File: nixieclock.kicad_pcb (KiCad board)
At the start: 2 copper layers, 146.5 x 85 mm, 56 parts, among them Q1 MMBTA42, Q2 FDS2672CT, Q3 SS8050, U1 UCC3803, U2 K155NA1, U3 PicoW, U4 K155NA1, U5 K155NA1, U6 K155NA1, U7 K155NA1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

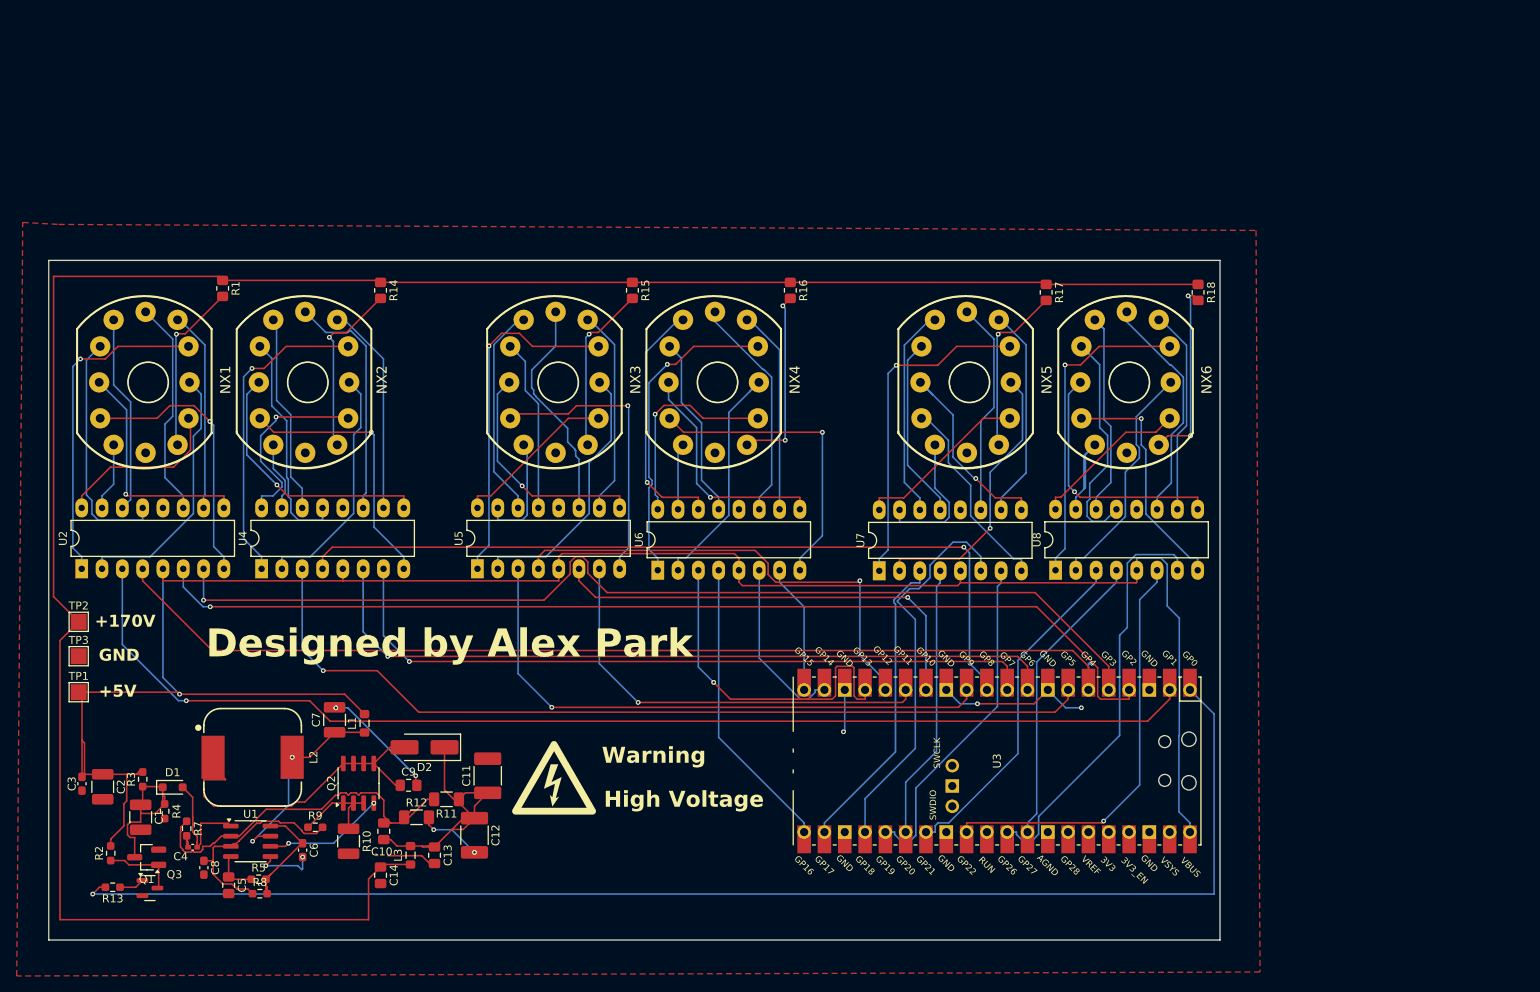
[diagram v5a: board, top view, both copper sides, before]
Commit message: updates to silk screen
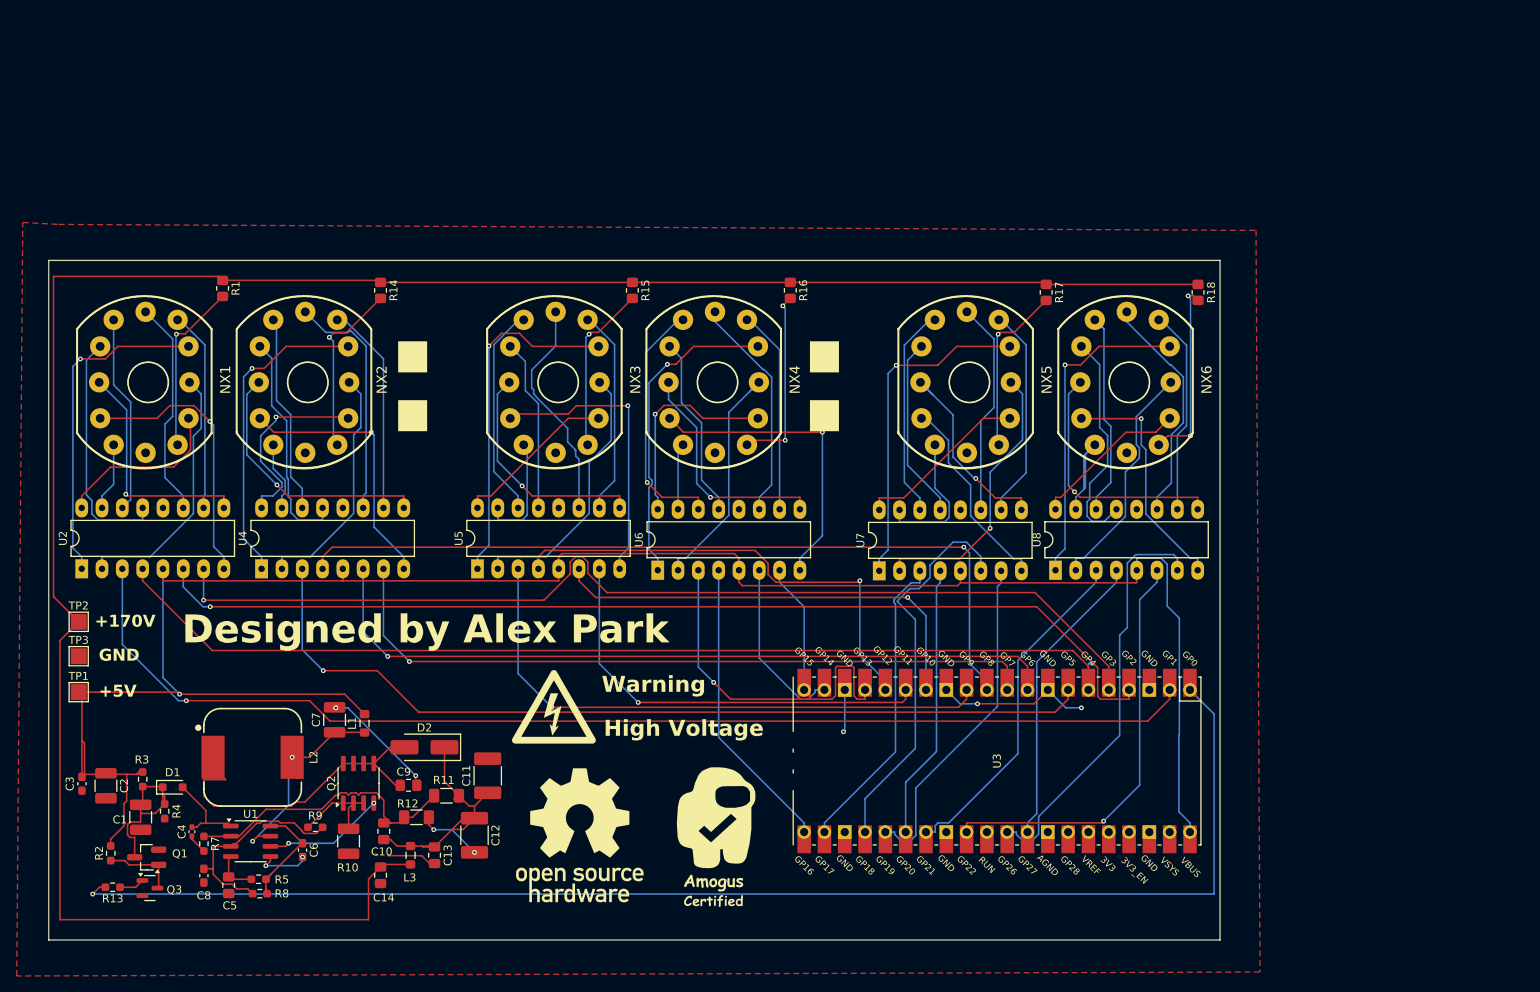
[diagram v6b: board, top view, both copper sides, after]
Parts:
- moved R7 2.87 mm to (98.0, 129.0)
- moved C4 1.95 mm to (96.5, 127.5), turned to -90 degrees
- moved C8 1.00 mm to (98.0, 133.0)
- moved R11 0.44 mm to (128.3, 123.0)
- moved C2 0.42 mm to (85.8, 121.8)
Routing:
- net Net-(U1-FB): track 46.1 -> 35.8 mm
- net Net-(D2-K): track 36.6 -> 29.4 mm
- net Net-(D1-A): track 16.1 -> 10.9 mm
- net Net-(D2-A): track 41.3 -> 38.9 mm
- net Net-(U6-3): track 30.3 -> 28.2 mm
- net Net-(U6-4): track 24.0 -> 21.9 mm
- net Net-(U8-3): track 32.9 -> 30.8 mm
- net Net-(U5-3): track 30.1 -> 28.0 mm
- net Net-(U4-9): track 31.1 -> 29.1 mm
- net Net-(U1-Vref): track 15.7 -> 13.8 mm
- net GND: track 61.5 -> 59.9 mm
- net Net-(NX6-PadA): track 24.3 -> 22.7 mm
- net Net-(U6-1): track 8.76 -> 7.44 mm
- net Net-(U8-6): track 29.7 -> 28.5 mm
- net Net-(U6-6): track 29.0 -> 27.7 mm
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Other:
- board text added: ":"

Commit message: small modifications to pcb
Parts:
- added C15: 0.1uF 16v, Capacitor_SMD:C_0603_1608Metric_Pad1.08x0.95mm_HandSolder, F.Cu at (95.0, 97.5)
- added C16: C16, Capacitor_SMD:C_0603_1608Metric_Pad1.08x0.95mm_HandSolder, F.Cu at (114.5, 97.2)
- added C17: 0.1uF 16v, Capacitor_SMD:C_0603_1608Metric_Pad1.08x0.95mm_HandSolder, F.Cu at (138.8, 97.2)
- added C18: C18, Capacitor_SMD:C_0603_1608Metric_Pad1.08x0.95mm_HandSolder, F.Cu at (179.0, 94.5)
- added C20: 0.1uF 16v, Capacitor_SMD:C_0603_1608Metric_Pad1.08x0.95mm_HandSolder, F.Cu at (214.8, 98.8)
- added D3: Green LED, LED_SMD:LED_0805_2012Metric_Pad1.15x1.40mm_HandSolder, F.Cu at (201.2, 135.5)
- added D4: LED_Filled, LED_SMD:LED_0805_2012Metric_Pad1.15x1.40mm_HandSolder, F.Cu at (126.5, 71.1)
- added D5: LED_Filled, LED_SMD:LED_0805_2012Metric_Pad1.15x1.40mm_HandSolder, F.Cu at (178.0, 71.1)
- added Q4: SS8050, Package_TO_SOT_SMD:SOT-23, F.Cu at (178.1, 81.8)
- added R19: 1k, Resistor_SMD:R_0603_1608Metric_Pad0.98x0.95mm_HandSolder, F.Cu at (197.3, 135.5)
- added R20: 140, Resistor_SMD:R_0603_1608Metric_Pad0.98x0.95mm_HandSolder, F.Cu at (181.2, 80.2)
- added R21: 1k, Resistor_SMD:R_0603_1608Metric_Pad0.98x0.95mm_HandSolder, F.Cu at (174.8, 81.8)
- added R22: 140, Resistor_SMD:R_0603_1608Metric_Pad0.98x0.95mm_HandSolder, F.Cu at (125.0, 81.8)
- R18: value R18 -> 10.5k
- moved L2 0.94 mm to (104.1, 117.2)
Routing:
- net +5V: track 260.6 -> 435.4 mm, vias 1 -> 3
- net +3V3: track 0.00 -> 72.3 mm, vias 0 -> 1
- net GPIO28: track 0.00 -> 71.5 mm, vias 0 -> 3
- net Net-(Q4-C): track 0.00 -> 63.8 mm
- net GND: track 59.9 -> 78.5 mm, vias 9 -> 13
- net Net-(D5-K): track 0.00 -> 9.86 mm
- net Net-(D4-K): track 0.00 -> 9.77 mm
- net Net-(D1-K): track 19.8 -> 25.4 mm
- net +170V: track 274.8 -> 269.8 mm
- net Net-(U6-1): track 7.44 -> 12.0 mm
- net Net-(D2-K): track 29.4 -> 33.5 mm
- net Net-(U5-1): track 13.8 -> 16.5 mm
- net Net-(U7-7): track 26.4 -> 29.1 mm
- net Net-(U5-7): track 25.6 -> 28.3 mm
- net Net-(U5-9): track 33.3 -> 35.8 mm
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- added copper zone on B.Cu, net +3V3
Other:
- outline, holes or cut-outs redrawn
- board text added: "Power"

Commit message: more random things
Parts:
- moved R22 6.32 mm to (127.0, 87.8)
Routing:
- net Net-(D4-K): track 9.77 -> 16.2 mm
- net Net-(Q4-C): track 63.8 -> 59.3 mm
- net +3V3: track 72.3 -> 68.5 mm
- net Net-(U7-3): track 26.8 -> 23.2 mm
- net +5V: track 435.4 -> 433.0 mm
- net Net-(D2-A): track 38.8 -> 36.4 mm
- net Net-(U2-0): track 22.4 -> 20.4 mm
- net Net-(NX5-PadA): track 22.6 -> 20.6 mm
- net Net-(NX3-PadA): track 22.2 -> 20.2 mm
- net Net-(NX1-PadA): track 22.6 -> 20.5 mm
- net Net-(U1-Vref): track 14.7 -> 12.8 mm
- net +170V: track 269.8 -> 268.0 mm
- net Net-(D2-K): track 33.5 -> 32.0 mm
- net Net-(U7-1): track 19.1 -> 17.8 mm
- net Net-(U8-6): track 29.4 -> 28.1 mm
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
